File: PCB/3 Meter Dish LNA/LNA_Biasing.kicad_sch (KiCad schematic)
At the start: 7 parts, among them U1 PMA2-63LN+

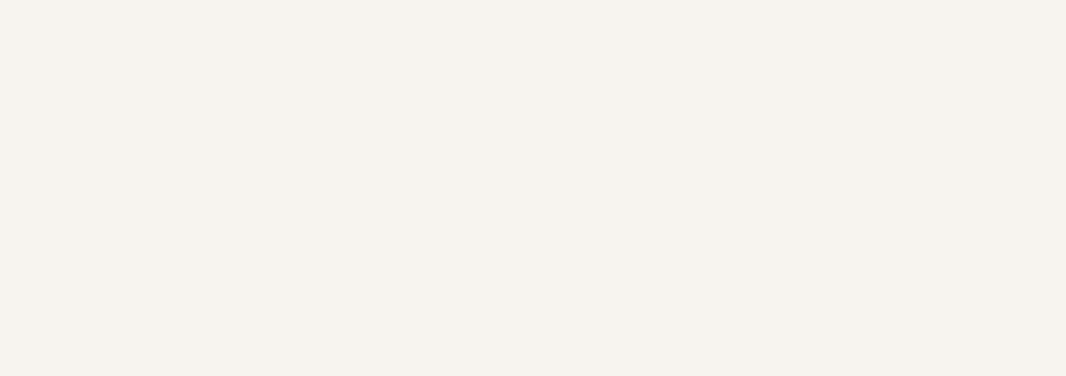
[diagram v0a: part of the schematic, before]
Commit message: PTH vias and mounting holes added
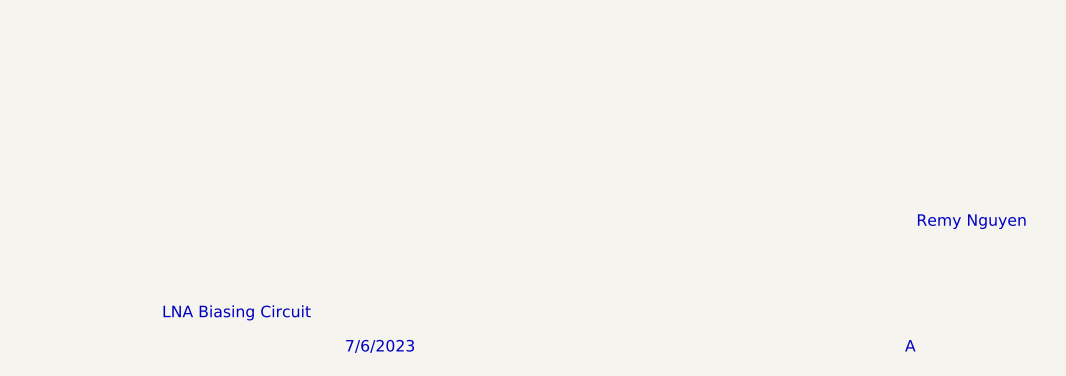
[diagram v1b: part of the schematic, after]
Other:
- note added: "7/6/2023"
- note added: "A"
- note added: "LNA Biasing Circuit"
- note added: "Remy Nguyen"
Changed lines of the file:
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@@
     (stroke (width 0) (type default))
+  )
+  (text "Remy Nguyen" (at 270.51 180.34 0)
+    (effects (font (size 1.27 1.27)) (justify left bottom))
+  )
+  (text "A" (at 269.24 194.31 0)
+    (effects (font (size 1.27 1.27)) (justify left bottom))
+  )
+  (text "7/6/2023" (at 207.01 194.31 0)
+    (effects (font (size 1.27 1.27)) (justify left bottom))
+  )
+  (text "LNA Biasing Circuit" (at 186.69 190.5 0)
+    (effects (font (size 1.27 1.27)) (justify left bottom))
   )
   (global_label "GND" (shape input) (at 170.18 105.41 0) (fields_autoplaced)
